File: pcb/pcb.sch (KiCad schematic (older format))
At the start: 24 parts, among them J1 USB_B_Micro, J2 AVR ISP connector, J3 Display connector, J4 Conn_01x02_Male, SW1 SSSS811101, SW2 SW_DIP_x01, SW3 SW_DIP_x01, U1 ATmega328P-AU, U2 MCP73831-2-OT, U3 AP9101CK6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

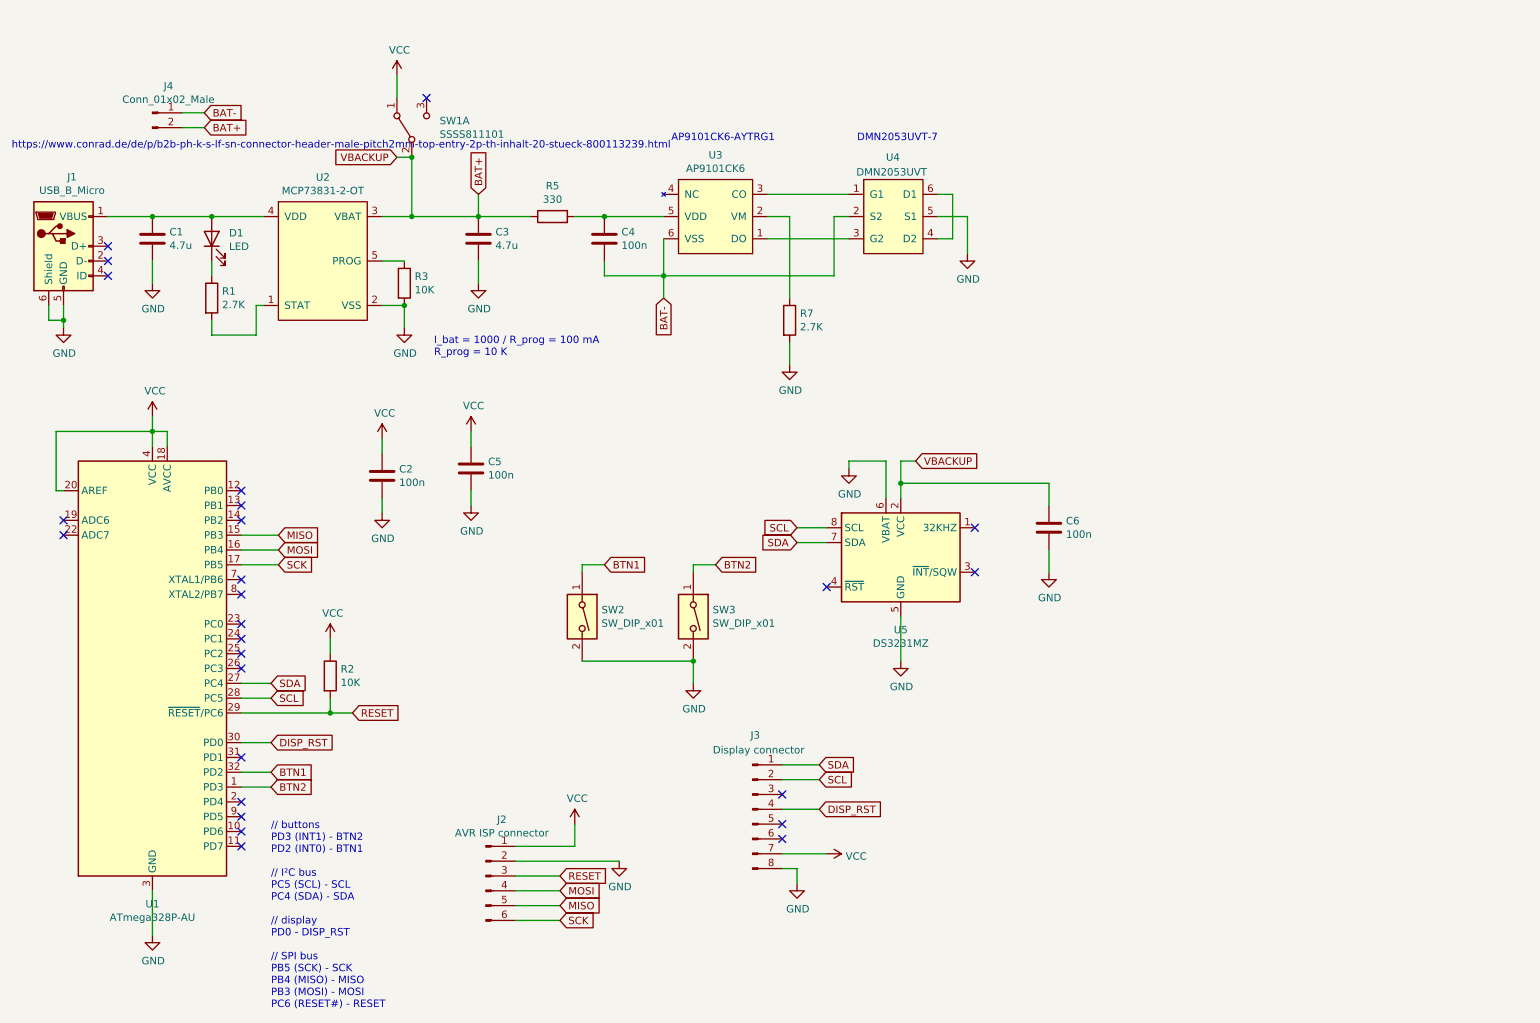
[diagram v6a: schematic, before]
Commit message: Changed TL3340 footprint
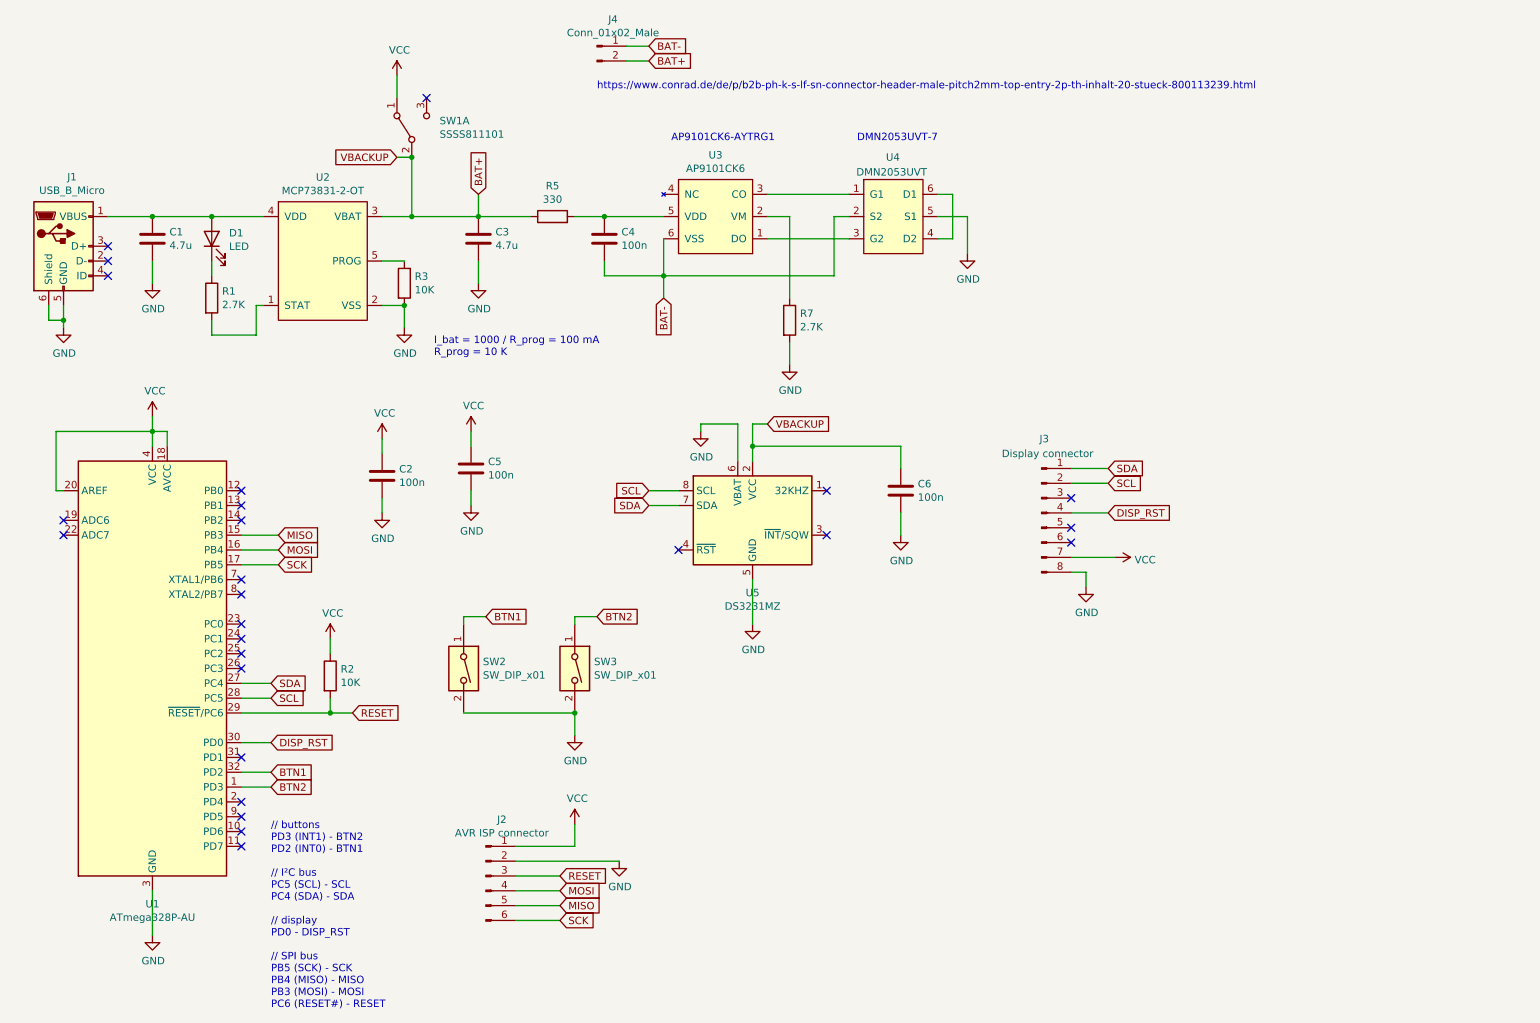
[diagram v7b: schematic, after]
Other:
- moved on the sheet: C6, J3, J4, SW2, SW3, U5
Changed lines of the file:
@@
 L Timer_RTC:DS3231MZ U5
 U 1 1 5E64F04B
-P 6850 4350
-F 0 "U5" H 6850 3861 50  0000 C CNN
-F 1 "DS3231MZ" H 6850 3770 50  0000 C CNN
-F 2 "Package_SO:SOIC-8_3.9x4.9mm_P1.27mm" H 6850 3850 50  0001 C CNN
-F 3 "http://datasheets.maximintegrated.com/en/ds/DS3231M.pdf" H 6850 3750 50  0001 C CNN
-	1    6850 4350
+P 5850 4100
+F 0 "U5" H 5850 3611 50  0000 C CNN
+F 1 "DS3231MZ" H 5850 3520 50  0000 C CNN
+F 2 "Package_SO:SOIC-8_3.9x4.9mm_P1.27mm" H 5850 3600 50  0001 C CNN
+F 3 "http://datasheets.maximintegrated.com/en/ds/DS3231M.pdf" H 5850 3500 50  0001 C CNN
+	1    5850 4100
 	1    0    0    -1
 $EndComp
@@
 L power:GND #PWR0107
 U 1 1 5E6C7611
-P 5450 5200
-F 0 "#PWR0107" H 5450 4950 50  0001 C CNN
-F 1 "GND" H 5455 5027 50  0000 C CNN
-F 2 "" H 5450 5200 50  0001 C CNN
-F 3 "" H 5450 5200 50  0001 C CNN
-	1    5450 5200
-	1    0    0    -1
-$EndComp
-Wire Wire Line
-	4700 5050 5450 5050
-Wire Wire Line
-	5450 5200 5450 5050
-Text GLabel 4850 4400 2    50   Input ~ 0
+P 4650 5550
+F 0 "#PWR0107" H 4650 5300 50  0001 C CNN
+F 1 "GND" H 4655 5377 50  0000 C CNN
+F 2 "" H 4650 5550 50  0001 C CNN
+F 3 "" H 4650 5550 50  0001 C CNN
+	1    4650 5550
+	1    0    0    -1
+$EndComp
+Wire Wire Line
+	3900 5400 4650 5400
+Wire Wire Line
+	4650 5550 4650 5400
+Text GLabel 4050 4750 2    50   Input ~ 0
 BTN1
-Text GLabel 5600 4400 2    50   Input ~ 0
+Text GLabel 4800 4750 2    50   Input ~ 0
 BTN2
 Wire Wire Line
-	4850 4400 4700 4400
-Wire Wire Line
-	4700 4400 4700 4450
-Wire Wire Line
-	5600 4400 5450 4400
-Wire Wire Line
-	5450 4400 5450 4450
-Text GLabel 6150 4150 0    50   Input ~ 0
+	4050 4750 3900 4750
+Wire Wire Line
+	3900 4750 3900 4800
+Wire Wire Line
+	4800 4750 4650 4750
+Wire Wire Line
+	4650 4750 4650 4800
+Text GLabel 5150 3900 0    50   Input ~ 0
 SCL
-Text GLabel 6150 4250 0    50   Input ~ 0
+Text GLabel 5150 4000 0    50   Input ~ 0
 SDA
 Wire Wire Line
-	6150 4250 6350 4250
-Wire Wire Line
-	6150 4150 6350 4150
+	5150 4000 5350 4000
+Wire Wire Line
+	5150 3900 5350 3900
 $Comp
 L power:GND #PWR0109
 U 1 1 5E6DC975
-P 6850 5050
-F 0 "#PWR0109" H 6850 4800 50  0001 C CNN
-F 1 "GND" H 6855 4877 50  0000 C CNN
-F 2 "" H 6850 5050 50  0001 C CNN
-F 3 "" H 6850 5050 50  0001 C CNN
-	1    6850 5050
-	1    0    0    -1
-$EndComp
-Wire Wire Line
-	6850 5050 6850 4750
+P 5850 4800
+F 0 "#PWR0109" H 5850 4550 50  0001 C CNN
+F 1 "GND" H 5855 4627 50  0000 C CNN
+F 2 "" H 5850 4800 50  0001 C CNN
+F 3 "" H 5850 4800 50  0001 C CNN
+	1    5850 4800
+	1    0    0    -1
+$EndComp
+Wire Wire Line
+	5850 4800 5850 4500
 $Comp
 L power:VCC #PWR0110
@@
 NoConn ~ 2400 4000
 NoConn ~ 2400 3900
-NoConn ~ 6350 4550
-NoConn ~ 7350 4450
-NoConn ~ 7350 4150
+NoConn ~ 5350 4300
+NoConn ~ 6350 4200
+NoConn ~ 6350 3900
 $Comp
 L Connector:Conn_01x06_Male J2
@@
 Wire Wire Line
 	4250 6800 4550 6800
-Text GLabel 6300 5850 2    50   Input ~ 0
+Text GLabel 8250 3850 2    50   Input ~ 0
 SCL
-Text GLabel 6300 5750 2    50   Input ~ 0
+Text GLabel 8250 3750 2    50   Input ~ 0
 SDA
 Wire Wire Line
-	6050 5850 6300 5850
-Wire Wire Line
-	6050 5750 6300 5750
+	8000 3850 8250 3850
+Wire Wire Line
+	8000 3750 8250 3750
 Text Notes 6000 1550 2    50   ~ 0
 AP9101CK6-AYTRG1
@@
 L Connector:Conn_01x08_Male J3
 U 1 1 5E7C51B2
-P 5850 6050
-F 0 "J3" H 5900 6550 50  0000 R CNN
-F 1 "Display connector" H 6200 6450 50  0000 R CNN
-F 2 "Connector_PinHeader_2.54mm:PinHeader_1x08_P2.54mm_Vertical" H 5850 6050 50  0001 C CNN
-F 3 "~" H 5850 6050 50  0001 C CNN
-	1    5850 6050
-	1    0    0    -1
-$EndComp
-Text GLabel 6300 6050 2    50   Input ~ 0
+P 7800 4050
+F 0 "J3" H 7850 4550 50  0000 R CNN
+F 1 "Display connector" H 8150 4450 50  0000 R CNN
+F 2 "Connector_PinHeader_2.54mm:PinHeader_1x08_P2.54mm_Vertical" H 7800 4050 50  0001 C CNN
+F 3 "~" H 7800 4050 50  0001 C CNN
+	1    7800 4050
+	1    0    0    -1
+$EndComp
+Text GLabel 8250 4050 2    50   Input ~ 0
 DISP_RST
 Wire Wire Line
-	6050 6050 6300 6050
-NoConn ~ 6050 5950
-NoConn ~ 6050 6150
-NoConn ~ 6050 6250
+	8000 4050 8250 4050
+NoConn ~ 8000 3950
+NoConn ~ 8000 4150
+NoConn ~ 8000 4250
 $Comp
 L power:GND #PWR0115
 U 1 1 5E7E1451
-P 6150 6550
-F 0 "#PWR0115" H 6150 6300 50  0001 C CNN
-F 1 "GND" H 6155 6377 50  0000 C CNN
-F 2 "" H 6150 6550 50  0001 C CNN
-F 3 "" H 6150 6550 50  0001 C CNN
-	1    6150 6550
-	1    0    0    -1
-$EndComp
-Wire Wire Line
-	6050 6450 6150 6450
-Wire Wire Line
-	6150 6450 6150 6550
+P 8100 4550
+F 0 "#PWR0115" H 8100 4300 50  0001 C CNN
+F 1 "GND" H 8105 4377 50  0000 C CNN
+F 2 "" H 8100 4550 50  0001 C CNN
+F 3 "" H 8100 4550 50  0001 C CNN
+	1    8100 4550
+	1    0    0    -1
+$EndComp
+Wire Wire Line
+	8000 4450 8100 4450
+Wire Wire Line
+	8100 4450 8100 4550
 $Comp
 L power:VCC #PWR0116
 U 1 1 5E7E39D9
-P 6350 6350
-F 0 "#PWR0116" H 6350 6200 50  0001 C CNN
-F 1 "VCC" V 6367 6478 50  0000 L CNN
-F 2 "" H 6350 6350 50  0001 C CNN
-F 3 "" H 6350 6350 50  0001 C CNN
-	1    6350 6350
+P 8300 4350
+F 0 "#PWR0116" H 8300 4200 50  0001 C CNN
+F 1 "VCC" V 8317 4478 50  0000 L CNN
+F 2 "" H 8300 4350 50  0001 C CNN
+F 3 "" H 8300 4350 50  0001 C CNN
+	1    8300 4350
 	0    1    1    0
 $EndComp
 Wire Wire Line
-	6050 6350 6350 6350
+	8000 4350 8300 4350
 Wire Wire Line
 	1500 2050 1800 2050
@@
 L power:GND #PWR0118
 U 1 1 5E7A9965
-P 6500 3750
-F 0 "#PWR0118" H 6500 3500 50  0001 C CNN
-F 1 "GND" H 6505 3577 50  0000 C CNN
-F 2 "" H 6500 3750 50  0001 C CNN
-F 3 "" H 6500 3750 50  0001 C CNN
-	1    6500 3750
-	1    0    0    -1
-$EndComp
-Wire Wire Line
-	6500 3750 6500 3700
-Wire Wire Line
-	6500 3700 6750 3700
-Wire Wire Line
-	6750 3700 6750 3950
-Text GLabel 6950 3700 2    50   Input ~ 0
+P 5500 3500
+F 0 "#PWR0118" H 5500 3250 50  0001 C CNN
+F 1 "GND" H 5505 3327 50  0000 C CNN
+F 2 "" H 5500 3500 50  0001 C CNN
+F 3 "" H 5500 3500 50  0001 C CNN
+	1    5500 3500
+	1    0    0    -1
+$EndComp
+Wire Wire Line
+	5500 3500 5500 3450
+Wire Wire Line
+	5500 3450 5750 3450
+Wire Wire Line
+	5750 3450 5750 3700
+Text GLabel 5950 3450 2    50   Input ~ 0
 VBACKUP
 Wire Wire Line
-	6850 3700 6850 3850
-Wire Wire Line
-	6850 3700 6950 3700
+	5850 3450 5850 3600
+Wire Wire Line
+	5850 3450 5950 3450
 $Comp
 L Device:R R1
@@
 L Switch:SW_DIP_x01 SW2
 U 1 1 5E72AEEF
-P 4700 4750
-F 0 "SW2" V 4654 4880 50  0000 L CNN
-F 1 "SW_DIP_x01" V 4745 4880 50  0000 L CNN
-F 2 "pcb:TL3340_SMT" H 4700 4750 50  0001 C CNN
-F 3 "~" H 4700 4750 50  0001 C CNN
-	1    4700 4750
+P 3900 5100
+F 0 "SW2" V 3854 5230 50  0000 L CNN
+F 1 "SW_DIP_x01" V 3945 5230 50  0000 L CNN
+F 2 "pcb:TL3340_SMT" H 3900 5100 50  0001 C CNN
+F 3 "~" H 3900 5100 50  0001 C CNN
+	1    3900 5100
 	0    1    1    0
 $EndComp
@@
 L Switch:SW_DIP_x01 SW3
 U 1 1 5E7385FA
-P 5450 4750
-F 0 "SW3" V 5404 4880 50  0000 L CNN
-F 1 "SW_DIP_x01" V 5495 4880 50  0000 L CNN
-F 2 "pcb:TL3340_SMT" H 5450 4750 50  0001 C CNN
-F 3 "~" H 5450 4750 50  0001 C CNN
-	1    5450 4750
+P 4650 5100
+F 0 "SW3" V 4604 5230 50  0000 L CNN
+F 1 "SW_DIP_x01" V 4695 5230 50  0000 L CNN
+F 2 "pcb:TL3340_SMT" H 4650 5100 50  0001 C CNN
+F 3 "~" H 4650 5100 50  0001 C CNN
+	1    4650 5100
 	0    1    1    0
 $EndComp
-Connection ~ 5450 5050
+Connection ~ 4650 5400
 $Comp
 L Device:C C5
@@
 L Device:C C6
 U 1 1 5E760DB3
-P 7850 4150
-F 0 "C6" H 7965 4196 50  0000 L CNN
-F 1 "100n" H 7965 4105 50  0000 L CNN
-F 2 "Capacitor_SMD:C_0603_1608Metric" H 7888 4000 50  0001 C CNN
-F 3 "~" H 7850 4150 50  0001 C CNN
-	1    7850 4150
+P 6850 3900
+F 0 "C6" H 6965 3946 50  0000 L CNN
+F 1 "100n" H 6965 3855 50  0000 L CNN
+F 2 "Capacitor_SMD:C_0603_1608Metric" H 6888 3750 50  0001 C CNN
+F 3 "~" H 6850 3900 50  0001 C CNN
+	1    6850 3900
 	1    0    0    -1
 $EndComp
@@
 L power:GND #PWR0121
 U 1 1 5E7615E0
-P 7850 4450
-F 0 "#PWR0121" H 7850 4200 50  0001 C CNN
-F 1 "GND" H 7855 4277 50  0000 C CNN
-F 2 "" H 7850 4450 50  0001 C CNN
-F 3 "" H 7850 4450 50  0001 C CNN
-	1    7850 4450
-	1    0    0    -1
-$EndComp
-Wire Wire Line
-	7850 4300 7850 4450
-Wire Wire Line
-	7850 4000 7850 3850
+P 6850 4200
+F 0 "#PWR0121" H 6850 3950 50  0001 C CNN
+F 1 "GND" H 6855 4027 50  0000 C CNN
+F 2 "" H 6850 4200 50  0001 C CNN
+F 3 "" H 6850 4200 50  0001 C CNN
+	1    6850 4200
+	1    0    0    -1
+$EndComp
+Wire Wire Line
+	6850 4050 6850 4200
+Wire Wire Line
+	6850 3750 6850 3600
 Wire Wire Line
 	1100 2650 1100 2750
@@
 L Connector:Conn_01x02_Male J4
 U 1 1 5E792C70
-P 1800 1350
-F 0 "J4" H 1908 1531 50  0000 C CNN
-F 1 "Conn_01x02_Male" H 1908 1440 50  0000 C CNN
-F 2 "Connector_JST:JST_PH_B2B-PH-K_1x02_P2.00mm_Vertical" H 1800 1350 50  0001 C CNN
-F 3 "~" H 1800 1350 50  0001 C CNN
-	1    1800 1350
-	1    0    0    -1
-$EndComp
-Text GLabel 2150 1450 2    50   Input ~ 0
+P 4800 900
+F 0 "J4" H 4908 1081 50  0000 C CNN
+F 1 "Conn_01x02_Male" H 4908 990 50  0000 C CNN
+F 2 "Connector_JST:JST_PH_B2B-PH-K_1x02_P2.00mm_Vertical" H 4800 900 50  0001 C CNN
+F 3 "~" H 4800 900 50  0001 C CNN
+	1    4800 900
+	1    0    0    -1
+$EndComp
+Text GLabel 5150 1000 2    50   Input ~ 0
 BAT+
-Text GLabel 2150 1350 2    50   Input ~ 0
+Text GLabel 5150 900  2    50   Input ~ 0
 BAT-
 Wire Wire Line
-	2150 1350 2000 1350
-Wire Wire Line
-	2000 1450 2150 1450
-Wire Wire Line
-	6850 3850 7850 3850
-Connection ~ 6850 3850
-Wire Wire Line
-	6850 3850 6850 3950
-Text Notes 850  1600 0    50   ~ 0
+	5150 900  5000 900
+Wire Wire Line
+	5000 1000 5150 1000
+Wire Wire Line
+	5850 3600 6850 3600
+Connection ~ 5850 3600
+Wire Wire Line
+	5850 3600 5850 3700
+Text Notes 4800 1200 0    50   ~ 0
 https://www.conrad.de/de/p/b2b-ph-k-s-lf-sn-connector-header-male-pitch2mm-top-entry-2p-th-inhalt-20-stueck-800113239.html
 $EndSCHEMATC

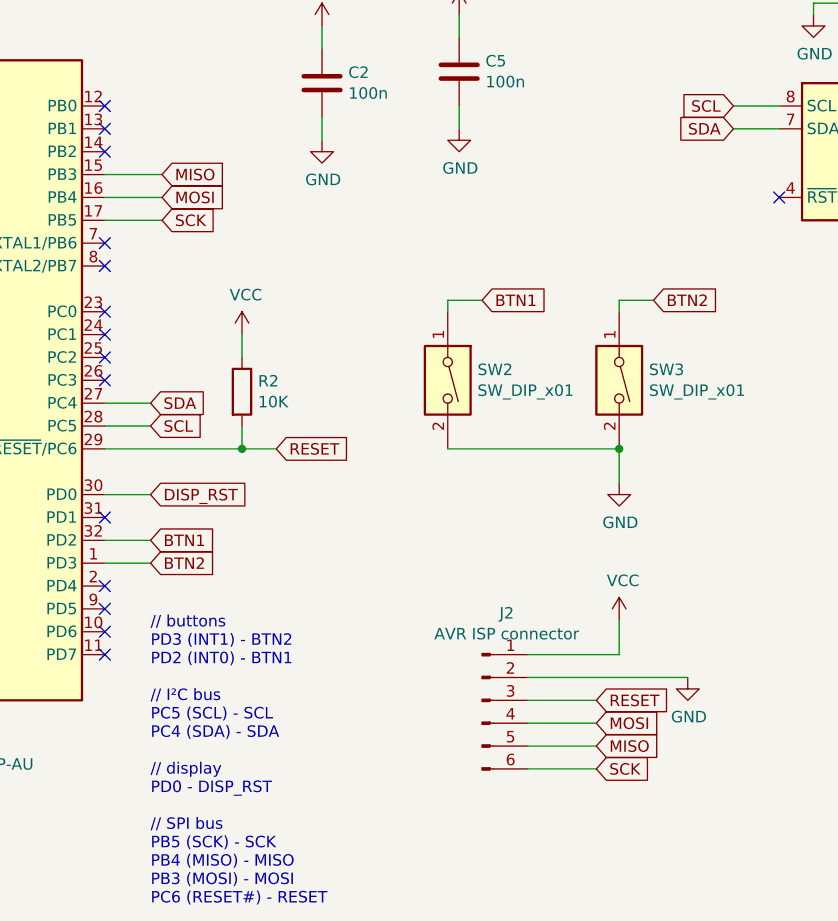
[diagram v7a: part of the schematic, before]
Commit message: Fixed MISO/MOSI mistake in PCB and schematic
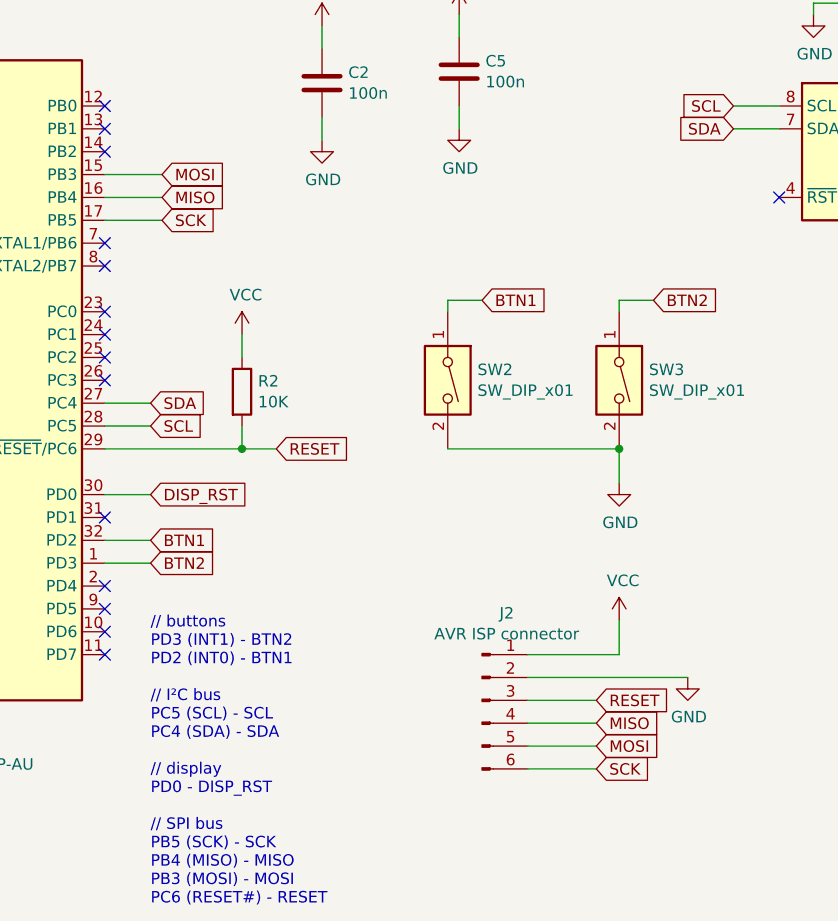
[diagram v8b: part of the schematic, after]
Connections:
- net MISO: now also J2.4 (Pin_4), U1.16 (PB4); no longer J2.5 (Pin_5), U1.15 (PB3)
- net MOSI: now also J2.5 (Pin_5), U1.15 (PB3); no longer J2.4 (Pin_4), U1.16 (PB4)
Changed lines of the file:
@@
 Wire Wire Line
 	2400 5200 2600 5200
+Text GLabel 2650 4300 2    50   Input ~ 0
+MISO
 Text GLabel 2650 4200 2    50   Input ~ 0
-MISO
-Text GLabel 2650 4300 2    50   Input ~ 0
 MOSI
 Text GLabel 2650 4400 2    50   Input ~ 0
@@
 Text GLabel 4550 6500 2    50   Input ~ 0
 RESET
+Text GLabel 4550 6700 2    50   Input ~ 0
+MOSI
 Text GLabel 4550 6600 2    50   Input ~ 0
-MOSI
-Text GLabel 4550 6700 2    50   Input ~ 0
 MISO
 Text GLabel 4550 6800 2    50   Input ~ 0
